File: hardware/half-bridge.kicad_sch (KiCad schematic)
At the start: 20 parts, among them J7 Phase_OUT, Q5 AGM015N10LL, Q6 AGM015N10LL, U3 IRS21867S, U4 INA240A2D

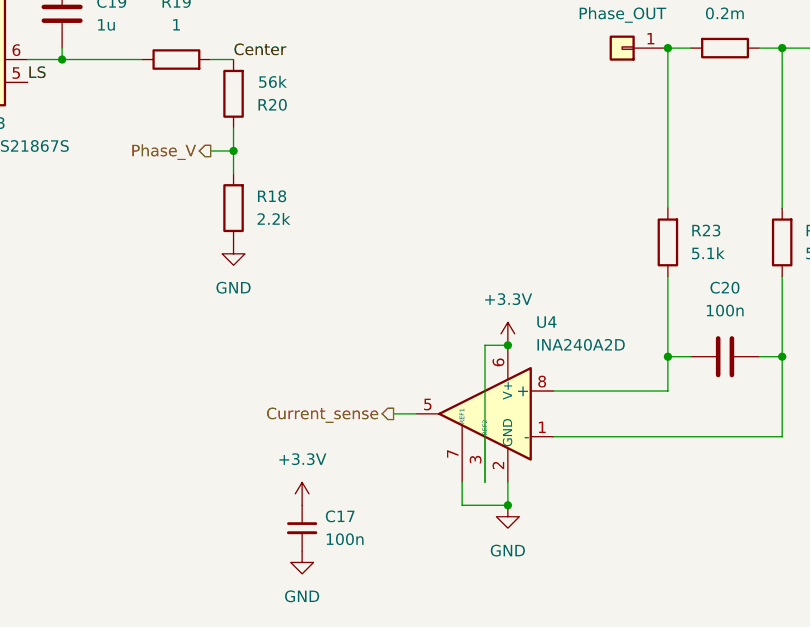
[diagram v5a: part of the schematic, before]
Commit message: Regulators layout
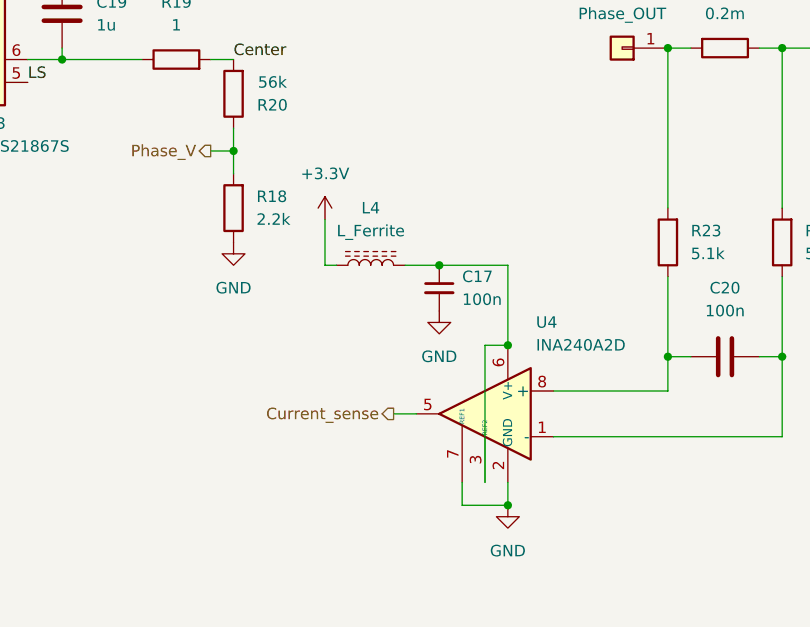
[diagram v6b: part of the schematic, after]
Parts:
- added L4: L_Ferrite, Inductor_SMD:L_0402_1005Metric, symbol Device:L_Ferrite
- C19: footprint Capacitor_SMD:C_0805_2012Metric -> Capacitor_SMD:C_1206_3216Metric
- R20: footprint Resistor_SMD:R_0402_1005Metric -> Resistor_SMD:R_0805_2012Metric
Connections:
- net +3.3V: now also L4.1; no longer C17.1, U4.3 (REF2), U4.6 (V+)
- new net: C17.1, L4.2, U4.3 (REF2), U4.6 (V+)
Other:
- moved on the sheet: C17
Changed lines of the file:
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@@
+	)
+	(junction
+		(at 129.54 114.3)
+		(diameter 0)
+		(color 0 0 0 0)
 	)
 	(junction
@@
 	)
 	(junction
-		(at 129.54 114.3)
-		(diameter 0)
-		(color 0 0 0 0)
-	)
-	(junction
 		(at 160.02 115.57)
 		(diameter 0)
@@
 	)
 	(junction
+		(at 121.92 105.41)
+		(diameter 0)
+		(color 0 0 0 0)
+	)
+	(junction
 		(at 182.88 97.79)
 		(diameter 0)
@@
 	(wire
 		(pts
+			(xy 129.54 105.41) (xy 129.54 114.3)
+		)
+		(stroke
+			(width 0)
+			(type default)
+		)
+	)
+	(wire
+		(pts
 			(xy 80.01 82.55) (xy 80.01 81.28)
 		)
@@
 	(wire
 		(pts
+			(xy 109.22 105.41) (xy 110.49 105.41)
+		)
+		(stroke
+			(width 0)
+			(type default)
+		)
+	)
+	(wire
+		(pts
 			(xy 182.88 97.79) (xy 190.5 97.79)
 		)
@@
 	(wire
 		(pts
+			(xy 118.11 105.41) (xy 121.92 105.41)
+		)
+		(stroke
+			(width 0)
+			(type default)
+		)
+	)
+	(wire
+		(pts
 			(xy 147.32 115.57) (xy 149.86 115.57)
 		)
@@
 		(pts
 			(xy 147.32 81.28) (xy 149.86 81.28)
+		)
+		(stroke
+			(width 0)
+			(type default)
+		)
+	)
+	(wire
+		(pts
+			(xy 109.22 100.33) (xy 109.22 105.41)
+		)
+		(stroke
+			(width 0)
+			(type default)
+		)
+	)
+	(wire
+		(pts
+			(xy 121.92 105.41) (xy 129.54 105.41)
 		)
 		(stroke
@@
 	(symbol
 		(lib_id "Device:C_Small")
-		(at 106.68 134.62 0)
+		(at 121.92 107.95 0)
 		(unit 1)
 		(exclude_from_sim no)
@@
 		(fields_autoplaced yes)
 		(property "Reference" "C17"
-			(at 109.22 133.3562 0)
+			(at 124.46 106.6862 0)
 			(effects
 				(font
@@
 		)
 		(property "Value" "100n"
-			(at 109.22 135.8962 0)
+			(at 124.46 109.2262 0)
 			(effects
 				(font
@@
 		)
 		(property "Footprint" "Capacitor_SMD:C_0402_1005Metric"
-			(at 106.68 134.62 0)
+			(at 121.92 107.95 0)
 			(effects
 				(font
@@
 		)
 		(property "Datasheet" "~"
-			(at 106.68 134.62 0)
+			(at 121.92 107.95 0)
 			(effects
 				(font
@@
 		)
 		(property "Description" "Unpolarized capacitor, small symbol"
-			(at 106.68 134.62 0)
+			(at 121.92 107.95 0)
 			(effects
 				(font
@@
 			)
 		)
-		(property "Footprint" "Resistor_SMD:R_0402_1005Metric"
+		(property "Footprint" "Resistor_SMD:R_0805_2012Metric"
 			(at 100.838 86.36 90)
 			(effects
@@
 	)
 	(symbol
-		(lib_id "power:+3.3V")
-		(at 129.54 114.3 0)
-		(unit 1)
-		(exclude_from_sim no)
-		(in_bom yes)
-		(on_board yes)
-		(dnp no)
-		(fields_autoplaced yes)
-		(property "Reference" "#PWR051"
-			(at 129.54 118.11 0)
-			(effects
-				(font
-					(size 1.27 1.27)
-				)
-				(hide yes)
-			)
-		)
-		(property "Value" "+3.3V"
-			(at 129.54 109.22 0)
-			(effects
-				(font
-					(size 1.27 1.27)
-				)
-			)
-		)
-		(property "Footprint" ""
-			(at 129.54 114.3 0)
-			(effects
-				(font
-					(size 1.27 1.27)
-				)
-				(hide yes)
-			)
-		)
-		(property "Datasheet" ""
-			(at 129.54 114.3 0)
-			(effects
-				(font
-					(size 1.27 1.27)
-				)
-				(hide yes)
-			)
-		)
-		(property "Description" "Power symbol creates a global label with name \"+3.3V\""
-			(at 129.54 114.3 0)
-			(effects
-				(font
-					(size 1.27 1.27)
-				)
-				(hide yes)
-			)
-		)
-		(pin "1"
-		)
-		(instances
-			(project "greenmobi-drive"
-				(path "/a12b77e7-bd0f-4a70-9ba2-19a87ce48819/4a5d7eb9-ddee-45d4-92b5-174bd9809dbc"
-					(reference "#PWR071")
-					(unit 1)
-				)
-				(path "/a12b77e7-bd0f-4a70-9ba2-19a87ce48819/caef660a-9a2f-49e8-a393-a85edb78ce64"
-					(reference "#PWR061")
-					(unit 1)
-				)
-				(path "/a12b77e7-bd0f-4a70-9ba2-19a87ce48819/cd601179-baef-4e34-b5da-beea03762ae5"
-					(reference "#PWR051")
-					(unit 1)
-				)
-			)
-		)
-	)
-	(symbol
 		(lib_id "Transistor_FET:Q_NMOS_GSD")
 		(at 180.34 90.17 0)
@@
 				(path "/a12b77e7-bd0f-4a70-9ba2-19a87ce48819/cd601179-baef-4e34-b5da-beea03762ae5"
 					(reference "Q6")
+					(unit 1)
+				)
+			)
+		)
+	)
+	(symbol
+		(lib_id "Device:L_Ferrite")
+		(at 114.3 105.41 90)
+		(unit 1)
+		(exclude_from_sim no)
+		(in_bom yes)
+		(on_board yes)
+		(dnp no)
+		(fields_autoplaced yes)
+		(property "Reference" "L4"
+			(at 114.3 99.06 90)
+			(effects
+				(font
+					(size 1.27 1.27)
+				)
+			)
+		)
+		(property "Value" "L_Ferrite"
+			(at 114.3 101.6 90)
+			(effects
+				(font
+					(size 1.27 1.27)
+				)
+			)
+		)
+		(property "Footprint" "Inductor_SMD:L_0402_1005Metric"
+			(at 114.3 105.41 0)
+			(effects
+				(font
+					(size 1.27 1.27)
+				)
+				(hide yes)
+			)
+		)
+		(property "Datasheet" "~"
+			(at 114.3 105.41 0)
+			(effects
+				(font
+					(size 1.27 1.27)
+				)
+				(hide yes)
+			)
+		)
+		(property "Description" "Inductor with ferrite core"
+			(at 114.3 105.41 0)
+			(effects
+				(font
+					(size 1.27 1.27)
+				)
+				(hide yes)
+			)
+		)
+		(pin "2"
+		)
+		(pin "1"
+		)
+		(instances
+			(project ""
+				(path "/a12b77e7-bd0f-4a70-9ba2-19a87ce48819/4a5d7eb9-ddee-45d4-92b5-174bd9809dbc"
+					(reference "L6")
+					(unit 1)
+				)
+				(path "/a12b77e7-bd0f-4a70-9ba2-19a87ce48819/caef660a-9a2f-49e8-a393-a85edb78ce64"
+					(reference "L5")
+					(unit 1)
+				)
+				(path "/a12b77e7-bd0f-4a70-9ba2-19a87ce48819/cd601179-baef-4e34-b5da-beea03762ae5"
+					(reference "L4")
 					(unit 1)
 				)
@@
 	(symbol
 		(lib_id "power:GND")
-		(at 106.68 137.16 0)
+		(at 121.92 110.49 0)
 		(unit 1)
 		(exclude_from_sim no)
@@
 		(fields_autoplaced yes)
 		(property "Reference" "#PWR066"
-			(at 106.68 143.51 0)
+			(at 121.92 116.84 0)
 			(effects
 				(font
@@
 		)
 		(property "Value" "GND"
-			(at 106.68 142.24 0)
+			(at 121.92 115.57 0)
 			(effects
 				(font
@@
 		)
 		(property "Footprint" ""
-			(at 106.68 137.16 0)
+			(at 121.92 110.49 0)
 			(effects
 				(font
@@
 		)
 		(property "Datasheet" ""
-			(at 106.68 137.16 0)
+			(at 121.92 110.49 0)
 			(effects
 				(font
@@
 		)
 		(property "Description" "Power symbol creates a global label with name \"GND\" , ground"
-			(at 106.68 137.16 0)
+			(at 121.92 110.49 0)
 			(effects
 				(font
@@
 			)
 		)
-		(property "Footprint" "Capacitor_SMD:C_0805_2012Metric"
+		(property "Footprint" "Capacitor_SMD:C_1206_3216Metric"
 			(at 80.9752 81.28 0)
 			(effects
@@
 	(symbol
 		(lib_id "power:+3.3V")
-		(at 106.68 132.08 0)
+		(at 109.22 100.33 0)
 		(unit 1)
 		(exclude_from_sim no)
@@
 		(fields_autoplaced yes)
 		(property "Reference" "#PWR045"
-			(at 106.68 135.89 0)
+			(at 109.22 104.14 0)
 			(effects
 				(font
@@
 		)
 		(property "Value" "+3.3V"
-			(at 106.68 127 0)
+			(at 109.22 95.25 0)
 			(effects
 				(font
@@
 		)
 		(property "Footprint" ""
-			(at 106.68 132.08 0)
+			(at 109.22 100.33 0)
 			(effects
 				(font
@@
 		)
 		(property "Datasheet" ""
-			(at 106.68 132.08 0)
+			(at 109.22 100.33 0)
 			(effects
 				(font
@@
 		)
 		(property "Description" "Power symbol creates a global label with name \"+3.3V\""
-			(at 106.68 132.08 0)
-			(effects
-				(font
+			(at 109.22 100.33 0)
+			(effects
+				(font

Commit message: Placement complete
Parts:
- R23, R25: value 5.1k -> 1
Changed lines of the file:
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@@
 			)
 		)
-		(property "Value" "5.1k"
+		(property "Value" "1"
 			(at 162.56 104.1399 0)
 			(effects
@@
 			)
 		)
-		(property "Value" "5.1k"
+		(property "Value" "1"
 			(at 149.86 104.1399 0)
 			(effects

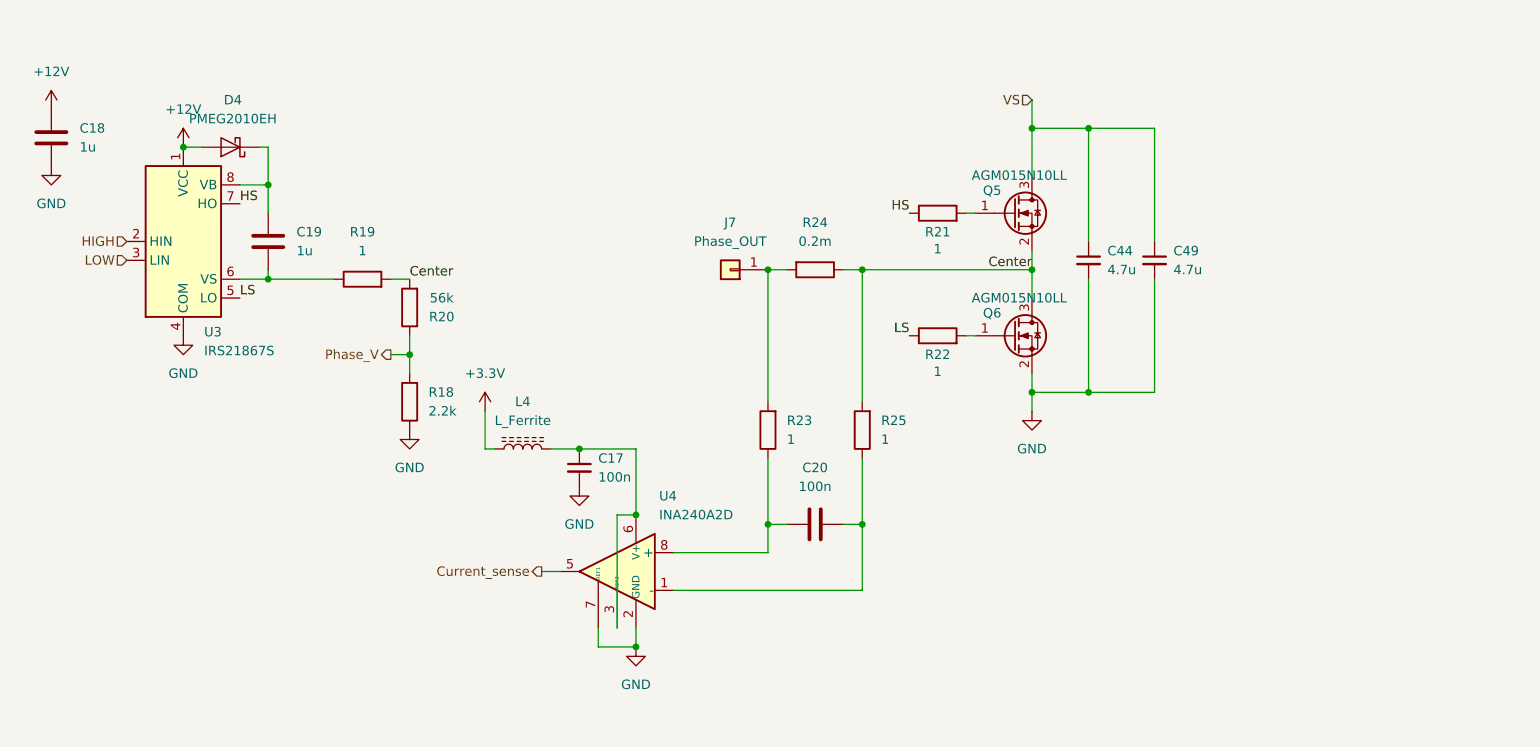
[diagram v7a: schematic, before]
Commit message: BOM optimizations
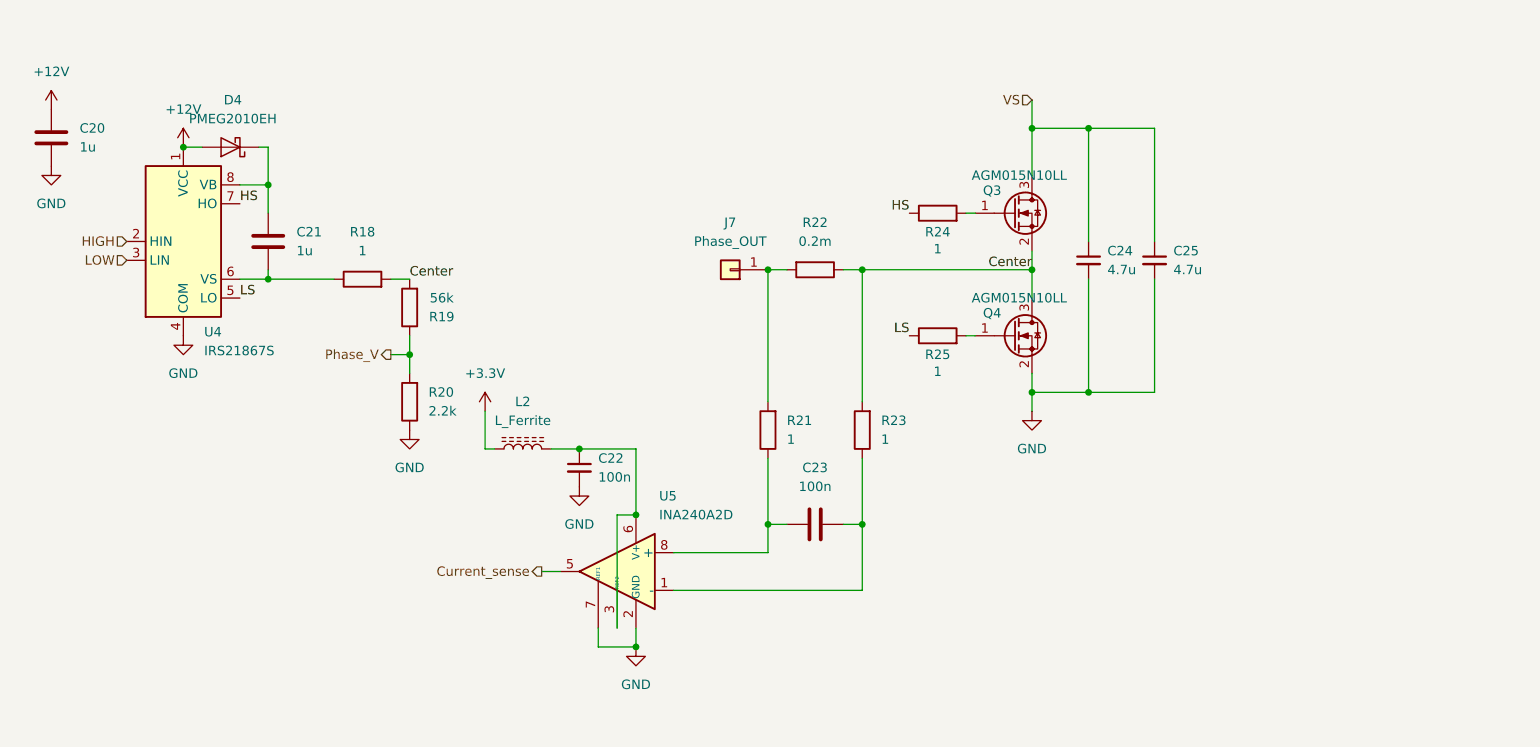
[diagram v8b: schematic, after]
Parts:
- renumbered C18 to C20, C19 to C21, C17 to C22, C20 to C23, C44 to C24, C49 to C25, L4 to L2, Q5 to Q3, Q6 to Q4, R19 to R18, R20 to R19, R18 to R20, R23 to R21, R24 to R22, R25 to R23, R21 to R24, R22 to R25, U3 to U4, U4 to U5
